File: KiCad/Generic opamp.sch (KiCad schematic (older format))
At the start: 21 parts, among them SW1 Switch_SPDT_x2

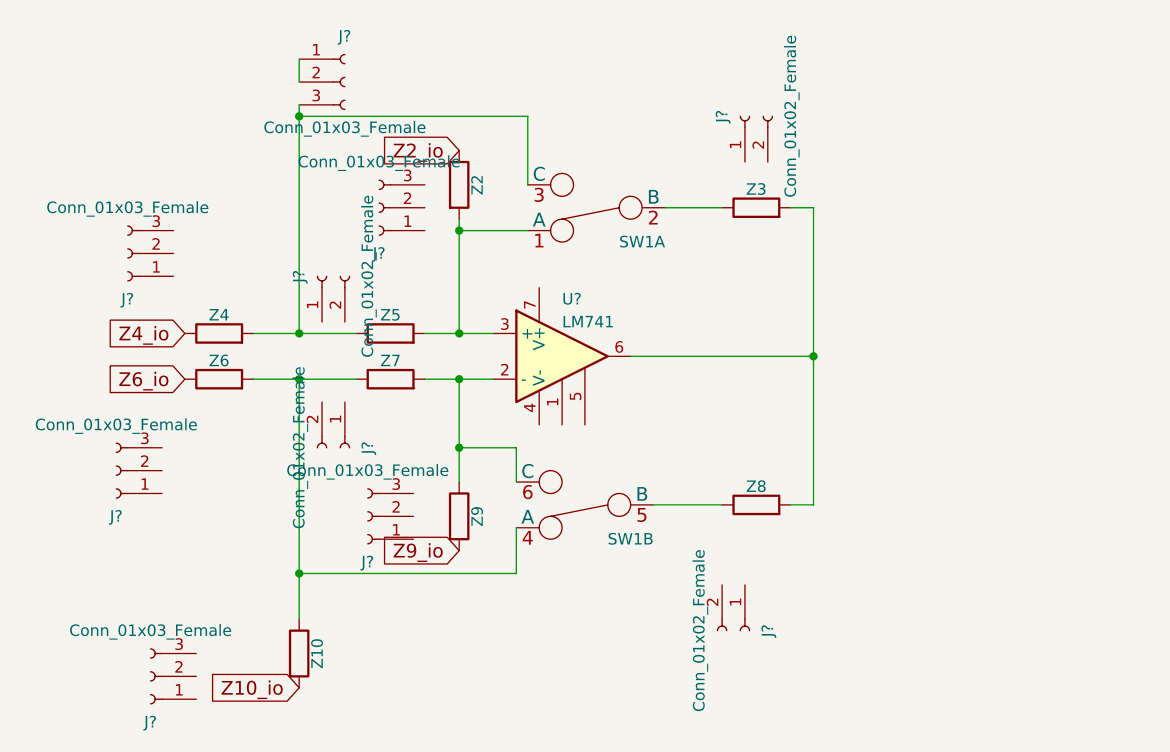
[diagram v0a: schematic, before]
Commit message: Replaced generic impedances with female headers.
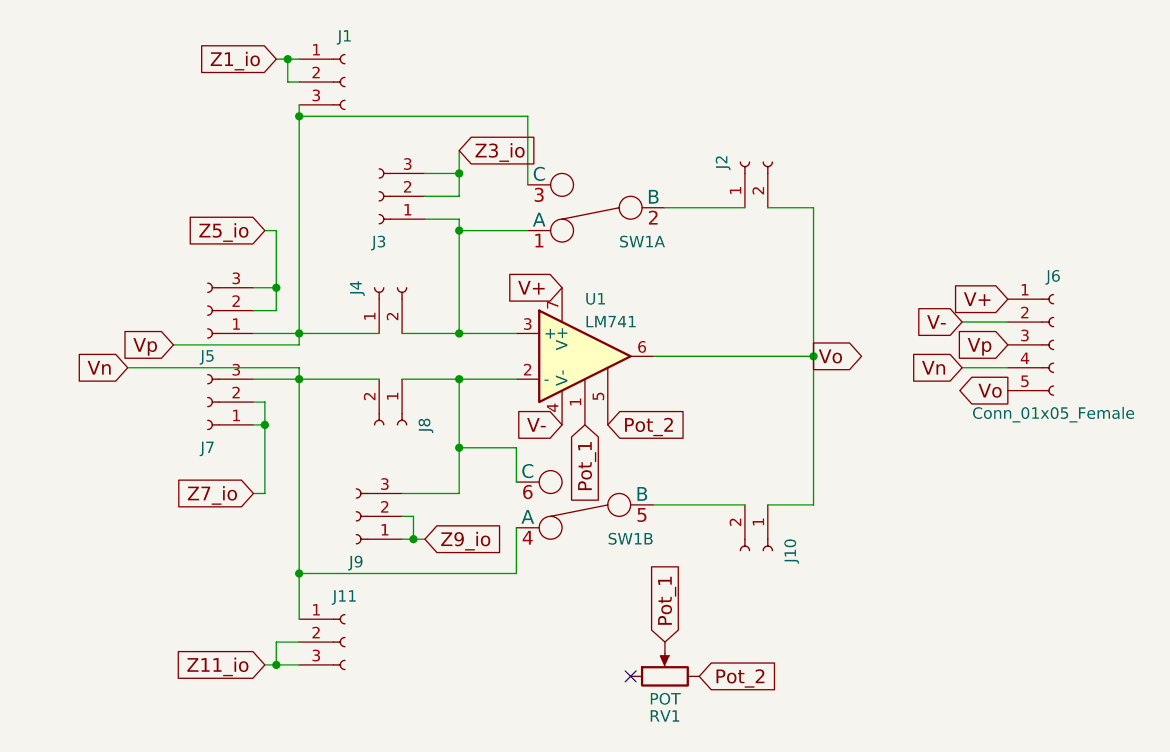
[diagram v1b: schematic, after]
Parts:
- removed Z10, Z2, Z3, Z4, Z5, Z6, Z7, Z8, Z9: R, symbol R
- added J6: Conn_01x05_Female, symbol Conn_01x05_Female
- added RV1: POT, symbol POT
- gave numbers to parts that had none: 11
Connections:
- net Z9_io: now also J9.1 (Pin_1), J9.2 (Pin_2)
- net Vp: now reaches J1.3 (Pin_3), SW1.3 (C)
- net Vp: now also J4.1 (Pin_1), J5.1 (Pin_1), J6.3 (Pin_3)
- net at SW1.6 (C), U1.2 (-): now also J8.1 (Pin_1), J9.3 (Pin_3)
- net at SW1.2 (B): now also J2.1 (Pin_1)
- net Vo: now reaches U1.6
- net Vo: now also J10.1 (Pin_1), J2.2 (Pin_2), J6.5 (Pin_5)
- net Vn: now reaches SW1.4 (A)
- net Vn: now also J11.1 (Pin_1), J7.3 (Pin_3), J8.2 (Pin_2), J6.4 (Pin_4)
- net at SW1.5 (B): now also J10.2 (Pin_2)
- net at SW1.1 (A), U1.3 (+): now also J3.1 (Pin_1), J4.2 (Pin_2)
- net Pot_1: now reaches U1.1
- net Pot_1: now also RV1.2
- net V-: now reaches U1.4 (V-)
- net V-: now also J6.2 (Pin_2)
- net Pot_2: now reaches U1.5
- net Pot_2: now also RV1.3
- net V+: now reaches U1.7 (V+)
- net V+: now also J6.1 (Pin_1)
- net Z1_io: now reaches J1.1 (Pin_1), J1.2 (Pin_2)
- net Z5_io: now reaches J5.2 (Pin_2)
- net Z5_io: now also J5.3 (Pin_3)
- net Z7_io: now reaches J7.1 (Pin_1)
- net Z7_io: now also J7.2 (Pin_2)
- net Z3_io: now reaches J3.2 (Pin_2)
- net Z3_io: now also J3.3 (Pin_3)
- net Z11_io: now reaches J11.2 (Pin_2)
- net Z11_io: now also J11.3 (Pin_3)
- no-connect marks 0 -> 1
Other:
- moved on the sheet: J10, J11, J2, J3, J4, J5, J7, J8, J9, U1
